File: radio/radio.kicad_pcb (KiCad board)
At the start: 4 copper layers, 63.5 x 63.5 mm, 23 parts, among them J1 SMA, J1001 CAS_stacking, U1 RFM69HCW, U2 74AHC1G04, U3 HMC544AE, U4 ublox_SAM-M8Q

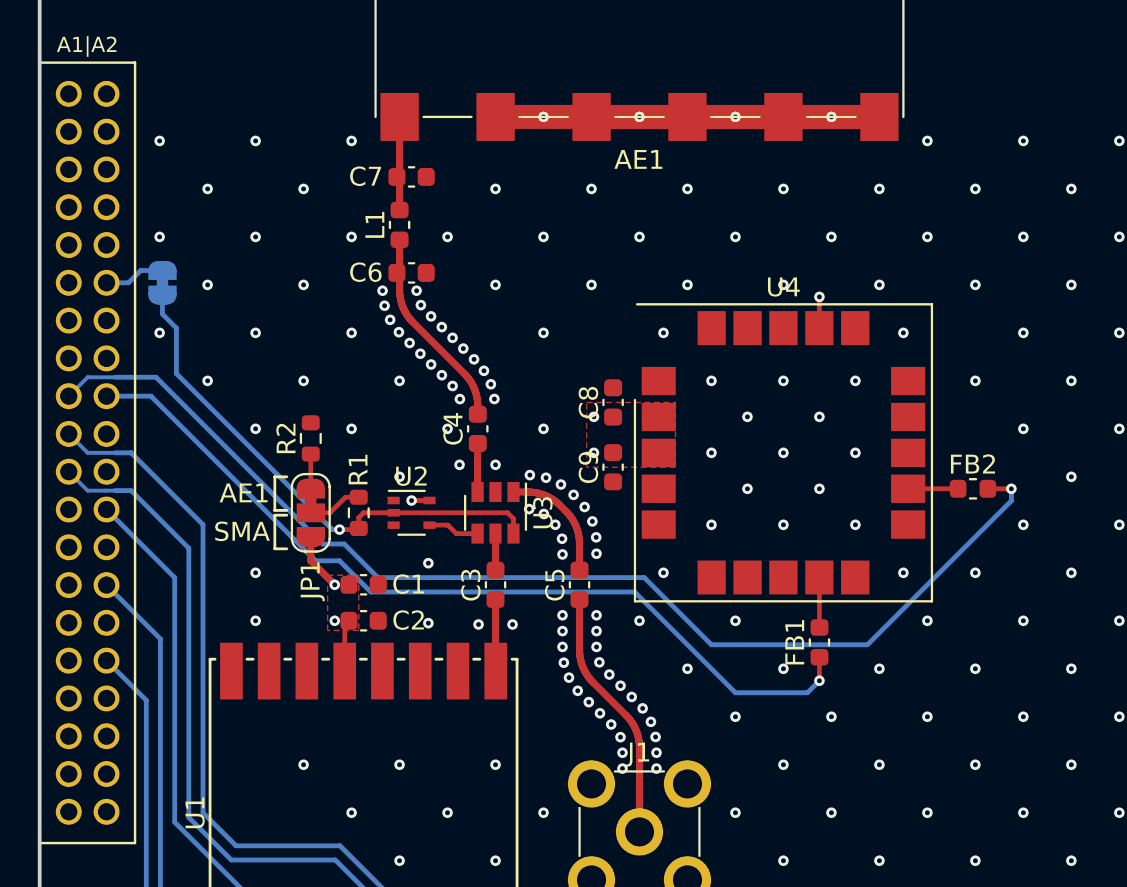
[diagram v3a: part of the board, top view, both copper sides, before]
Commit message: tweaked traces
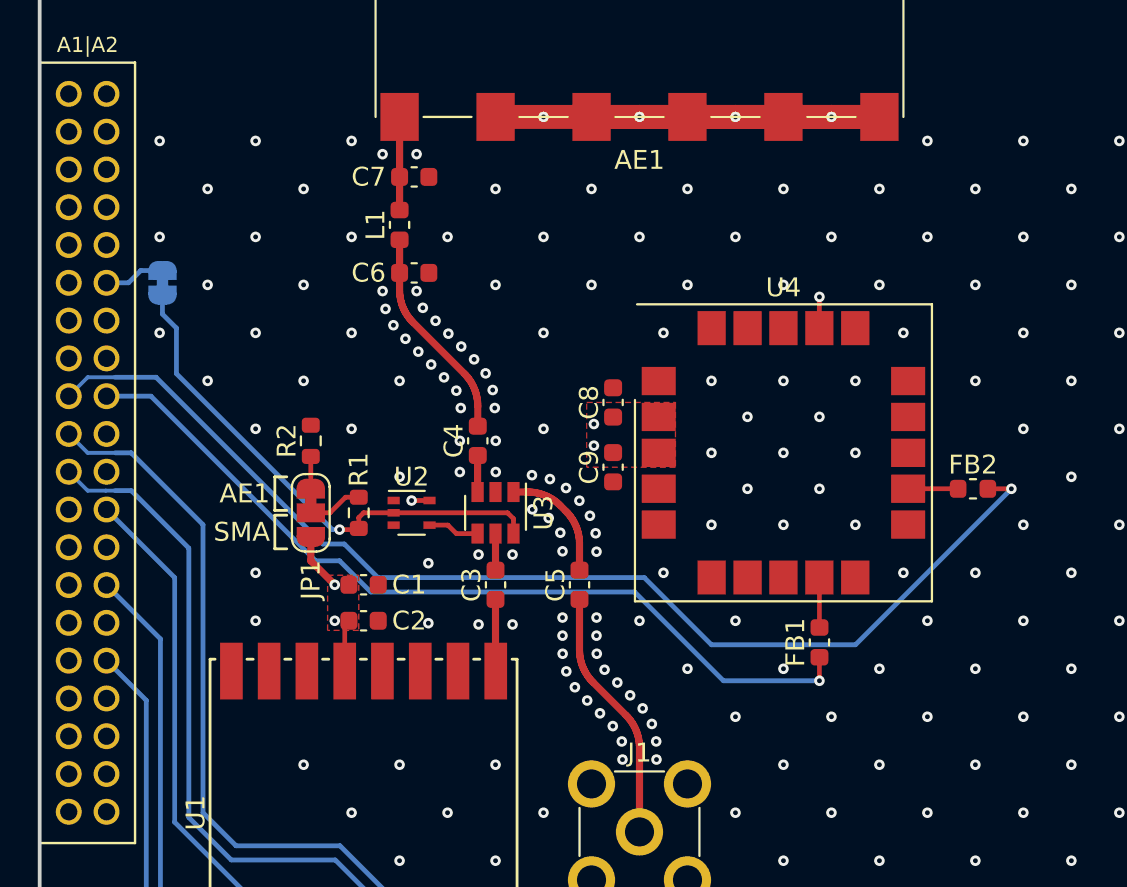
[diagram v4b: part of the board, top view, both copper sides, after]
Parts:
- moved C4 0.63 mm to (23.2, 31.1)
- moved C6 0.14 mm to (19.8, 22.2)
- moved C7 0.14 mm to (19.8, 17.1)
- moved R2 0.13 mm to (14.4, 31.1)
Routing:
- net Net-(C4-Pad1): track 10.9 -> 11.5 mm
- net Net-(C4-Pad2): track 2.57 -> 1.94 mm
- net +3V3: track 76.1 -> 76.7 mm
- net /SDA: track 45.7 -> 45.2 mm
- net GND: vias 197 -> 194

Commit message: Add test pins
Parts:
- added G***: LOGO, star-common-lib:star, F.Cu at (11.4, 5.08)
- added J2: Conn_01x04_Male, Connector_PinHeader_2.54mm:PinHeader_1x04_P2.54mm_Vertical_SMD_Pin1Left, F.Cu at (41.9, 58.4)
- added J3: Conn_01x02_Male, Connector_PinHeader_2.54mm:PinHeader_1x02_P2.54mm_Vertical_SMD_Pin1Left, F.Cu at (52.1, 58.4)
- R1, R2: value 1k -> 10k
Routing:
- net Net-(J2-Pad4): track 0.00 -> 62.3 mm, vias 0 -> 2
- net Net-(J2-Pad1): track 0.00 -> 49.8 mm, vias 0 -> 2
- net Net-(J3-Pad2): track 0.00 -> 37.8 mm
- net Net-(J2-Pad2): track 0.00 -> 32.1 mm
- net Net-(J3-Pad1): track 0.00 -> 30.7 mm
- net Net-(J2-Pad3): track 0.00 -> 18.9 mm
- net GND: vias 194 -> 193

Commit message: moved logo to silkscreen, shifted over debug connector for gps and added silkscreen
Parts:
- removed the G*** at (11.4, 5.08)
- added G***: LOGO, star-common-lib:star_7x6, F.Cu at (128.3, 71.6)
- moved J2 134.6 mm to (158.8, 125.2)
- moved AE1 133.7 mm to (147.6, 80.8)
- moved C3 133.7 mm to (140.0, 105.5)
- moved JP1 133.7 mm to (130.2, 101.7)
- moved R1 133.7 mm to (132.7, 101.7)
- moved R2 133.7 mm to (130.2, 97.9)
- moved U3 133.7 mm to (140.0, 101.7)
- moved C1 133.7 mm to (133.0, 105.5)
- moved C2 133.7 mm to (133.0, 107.4)
- moved C4 133.7 mm to (139.0, 97.9)
- moved C5 133.7 mm to (144.4, 105.5)
- moved C6 133.7 mm to (135.6, 89.0)
- moved C7 133.7 mm to (135.6, 83.9)
- moved C8 133.7 mm to (146.2, 95.9)
- moved C9 133.7 mm to (146.2, 99.3)
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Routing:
- net Net-(J2-Pad2): track 32.1 -> 26.2 mm
- net GND: vias 193 -> 191
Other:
- board text added: "EXTINT"
- board text added: "RESET"
- board text added: "RX"
- board text added: "SAFEBOOT"
- board text added: "TIMEPULSE"
- board text added: "TX"
